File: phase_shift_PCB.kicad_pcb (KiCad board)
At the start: 2 copper layers, 9.5 x 9.5 mm, 18 parts, among them J1 132414, J2 132414, J3 Conn_01x01_Socket, J4 Conn_01x01_Socket, J5 Conn_01x01_Pin, J6 Conn_01x01_Pin, U1 OPA2134, U2 LM13700, U3 LM334M

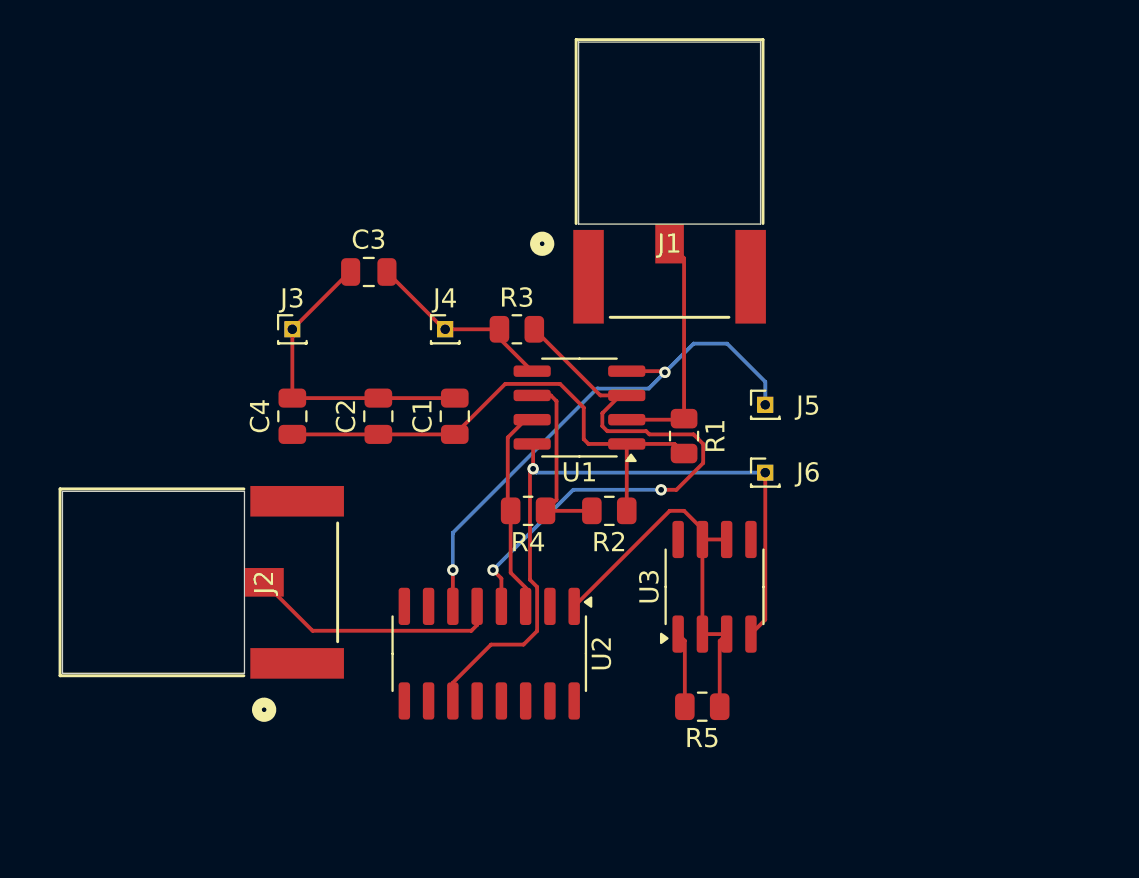
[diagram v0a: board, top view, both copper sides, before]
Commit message: Added digipots to schematic
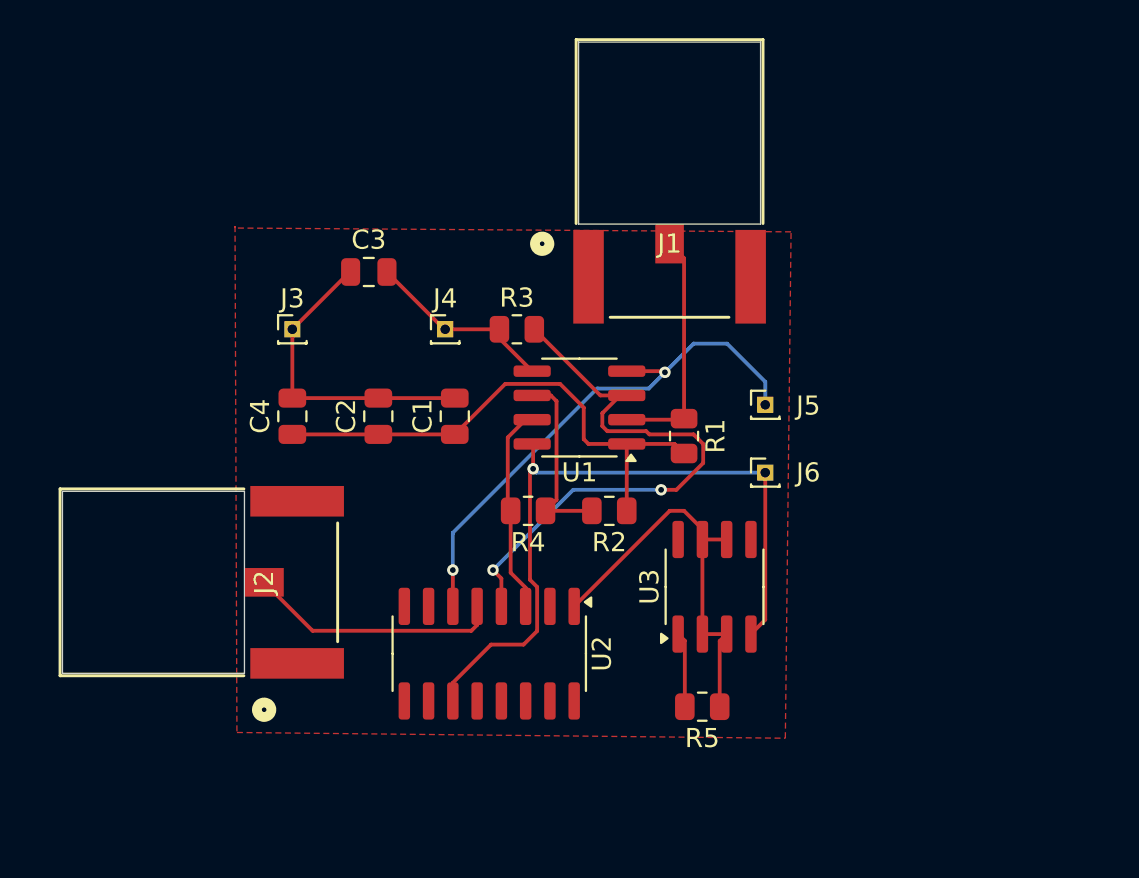
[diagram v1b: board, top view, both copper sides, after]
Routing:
- added copper zone on F.Cu, net GND
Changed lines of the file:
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@@
 		(net 22)
+	)
+	(zone
+		(net 3)
+		(net_name "GND")
+		(layer "F.Cu")
+		(hatch edge 0.5)
+		(connect_pads
+			(clearance 0.5)
+		)
+		(min_thickness 0.25)
+		(filled_areas_thickness no)
+		(fill yes
+			(thermal_gap 0.5)
+			(thermal_bridge_width 0.5)
+		)
+		(polygon
+			(pts
+				(xy 30.5 59.6) (xy 30.6 86.1) (xy 59.3 86.4) (xy 59.6 59.9) (xy 30.5 59.7)
+			)
+		)
 	)
 	(embedded_fonts no)

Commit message: PCB pretty much finished
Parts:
- removed R3: 1000, Resistor_SMD:R_0805_2012Metric
- added C5: 100n, Capacitor_SMD:C_0805_2012Metric, F.Cu at (44.4, 73.5)
- added C6: 100n, Capacitor_SMD:C_0805_2012Metric, F.Cu at (54.2, 68.3)
- added C7: 100n, Capacitor_SMD:C_0805_2012Metric, F.Cu at (41.0, 77.0)
- added C8: 100n, Capacitor_SMD:C_0805_2012Metric, F.Cu at (42.9, 87.0)
- added J10: Conn_01x01_Socket, Connector_PinHeader_1.00mm:PinHeader_1x01_P1.00mm_Vertical, F.Cu at (46.4, 57.4)
- added J11: Conn_01x01_Socket, Connector_PinHeader_1.00mm:PinHeader_1x01_P1.00mm_Vertical, F.Cu at (49.4, 57.4)
- added J12: Conn_01x01_Socket, Connector_PinHeader_1.00mm:PinHeader_1x01_P1.00mm_Vertical, F.Cu at (52.3, 57.4)
- added J13: Conn_01x01_Socket, Connector_PinHeader_1.00mm:PinHeader_1x01_P1.00mm_Vertical, F.Cu at (55.2, 57.4)
- added J5: Conn_01x01_Pin, Connector_PinHeader_1.00mm:PinHeader_1x01_P1.00mm_Vertical, F.Cu at (62.1, 73.1)
- added J8: Conn_01x01_Socket, Connector_PinHeader_1.00mm:PinHeader_1x01_P1.00mm_Vertical, F.Cu at (40.6, 57.4)
- added J9: Conn_01x01_Socket, Connector_PinHeader_1.00mm:PinHeader_1x01_P1.00mm_Vertical, F.Cu at (43.5, 57.4)
- added U4: AD8400ARZ10-REEL, Library:SOIC127P600X175-8N, F.Cu at (52.8, 62.5)
- added U5: AD8400ARZ1-REEL, Library:SOIC127P600X175-8N, F.Cu at (43.7, 62.5)
- moved J1 16.0 mm to (66.6, 65.8), turned to -90 degrees
- moved J6 7.90 mm to (62.1, 75.8)
- moved J7 7.21 mm to (62.1, 78.6)
- moved R5 5.47 mm to (58.7, 80.8), turned to -90 degrees
- moved R4 5.02 mm to (43.6, 70.0), turned to -90 degrees
- moved J4 3.54 mm to (38.1, 66.0)
- moved U3 2.50 mm to (53.7, 80.1), turned to 180 degrees
- moved C1 2.42 mm to (39.8, 70.6)
- moved C2 2.42 mm to (35.8, 70.5)
- moved C3 2.42 mm to (35.3, 63.0)
- moved C4 2.42 mm to (31.3, 70.5)
- moved J3 2.42 mm to (31.3, 66.0)
- moved R2 0.89 mm to (50.0, 73.6)
- moved U1 0.71 mm to (48.5, 69.8)
- moved R1 0.71 mm to (54.0, 71.3)
- renumbered J5 to J6, J6 to J7
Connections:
- net Net-(J4-Pin_1) renamed /W1
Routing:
- net +15V: track 37.6 -> 4.66 mm, vias 1 -> 0
- net GND: track 30.7 -> 0.00 mm, vias 2 -> 0
- net -15V: track 28.4 -> 6.82 mm, vias 2 -> 1
- net +5V: track 0.00 -> 16.3 mm, vias 0 -> 2
- net Net-(R5-Pad1): track 21.2 -> 5.71 mm
- net CLK: track 0.00 -> 14.3 mm
- net Net-(C1-Pad1): track 27.6 -> 13.6 mm
- net Net-(J2-Pad1): track 13.3 -> 0.00 mm
- net SDI: track 0.00 -> 12.8 mm, vias 0 -> 2
- net /W2: track 0.00 -> 11.1 mm
- net Net-(U1A--): track 12.5 -> 3.02 mm
- net Net-(J9-Pin_1): track 0.00 -> 9.21 mm
- net Net-(U2C-+): track 10.9 -> 2.65 mm
- net /W1: track 10.0 -> 17.3 mm
- net Net-(J11-Pin_1): track 0.00 -> 6.45 mm
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- removed copper zone on F.Cu, net GND

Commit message: .
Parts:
- J1, J2: value 132414 -> SMA-J-P-H-ST-EM1
- moved R1 0.50 mm to (53.5, 71.3)
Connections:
- J1 pad 2: (no net) -> GND
- J1 pad 3: (no net) -> GND
- J2 pad 2: (no net) -> GND
- J2 pad 3: (no net) -> GND
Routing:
- net +15V: track 4.66 -> 38.1 mm, vias 0 -> 2
- net -15V: track 6.82 -> 36.1 mm, vias 1 -> 2
- net Net-(C1-Pad1): track 13.6 -> 30.3 mm
- net Net-(J2-Pad1): track 0.00 -> 13.4 mm
- net Net-(U1A--): track 3.02 -> 14.1 mm
- net Net-(U2C-+): track 2.65 -> 13.3 mm
- net Net-(R5-Pad1): track 5.71 -> 13.2 mm
- net /W1: vias 0 -> 2
- net GND: vias 0 -> 105
- added copper zone on B.Cu, net GND
- added copper zone on F.Cu, net GND
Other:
- board size 9.5 x 9.5 mm -> 40 x 38.5 mm
- board text added: "+15V"
- board text added: "-15V"
- board text added: "5V"
- board text added: "CLK"
- board text added: "CS1"
- board text added: "CS2"
- board text added: "Dihan Wu & Hiro Shiraishi"
- board text added: "GND"
- board text added: "OPT"
- board text added: "Phase Shift PCB V1.0"
- board text added: "SDI"

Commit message: .
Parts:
- removed J10, J11, J12, J13, J9: Conn_01x01_Socket, Connector_PinHeader_1.00mm:PinHeader_1x01_P1.00mm_Vertical
- J3, J4: value Conn_01x01_Socket -> Conn_01x01_Pin; footprint Connector_PinHeader_1.00mm:PinHeader_1x01_P1.00mm_Vertical -> Connector_PinHeader_2.54mm:PinHeader_1x01_P2.54mm_Vertical
- J5, J6, J7: footprint Connector_PinHeader_1.00mm:PinHeader_1x01_P1.00mm_Vertical -> Connector_PinHeader_2.54mm:PinHeader_1x01_P2.54mm_Vertical
- J8: value Conn_01x01_Socket -> Conn_01x06_Pin; footprint Connector_PinHeader_1.00mm:PinHeader_1x01_P1.00mm_Vertical -> Connector_PinSocket_2.54mm:PinSocket_1x06_P2.54mm_Vertical
- moved J7 6.21 mm to (65.5, 83.8)
- moved J6 4.63 mm to (65.5, 79.0)
- moved J5 3.57 mm to (65.5, 74.2)
- moved J8 3.01 mm to (41.7, 54.6), turned to 90 degrees
- moved C3 1.80 mm to (34.3, 61.5)
- moved J3 1.28 mm to (30.5, 65.0)
- moved J4 1.00 mm to (38.0, 65.0)
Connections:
- U4 pad 3: Net-(J12-Pin_1) -> CS2
- U5 pad 3: Net-(J10-Pin_1) -> CS1
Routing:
- net CS2: track 0.00 -> 9.97 mm
- net Net-(J12-Pin_1): track 9.21 -> 0.00 mm
- net CS1: track 0.00 -> 8.80 mm
- net Net-(J10-Pin_1): track 6.45 -> 0.00 mm
- net +15V: track 38.1 -> 43.8 mm
- net -15V: track 36.1 -> 40.8 mm
- net +5V: track 16.3 -> 18.8 mm
- net SDI: track 12.8 -> 15.3 mm
- net Net-(J3-Pin_1): track 16.4 -> 18.1 mm
- net /W1: track 17.3 -> 17.9 mm
- net CLK: track 14.3 -> 14.5 mm, vias 0 -> 2
- net GND: vias 105 -> 81
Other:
- board size 40 x 38.5 mm -> 40 x 39 mm

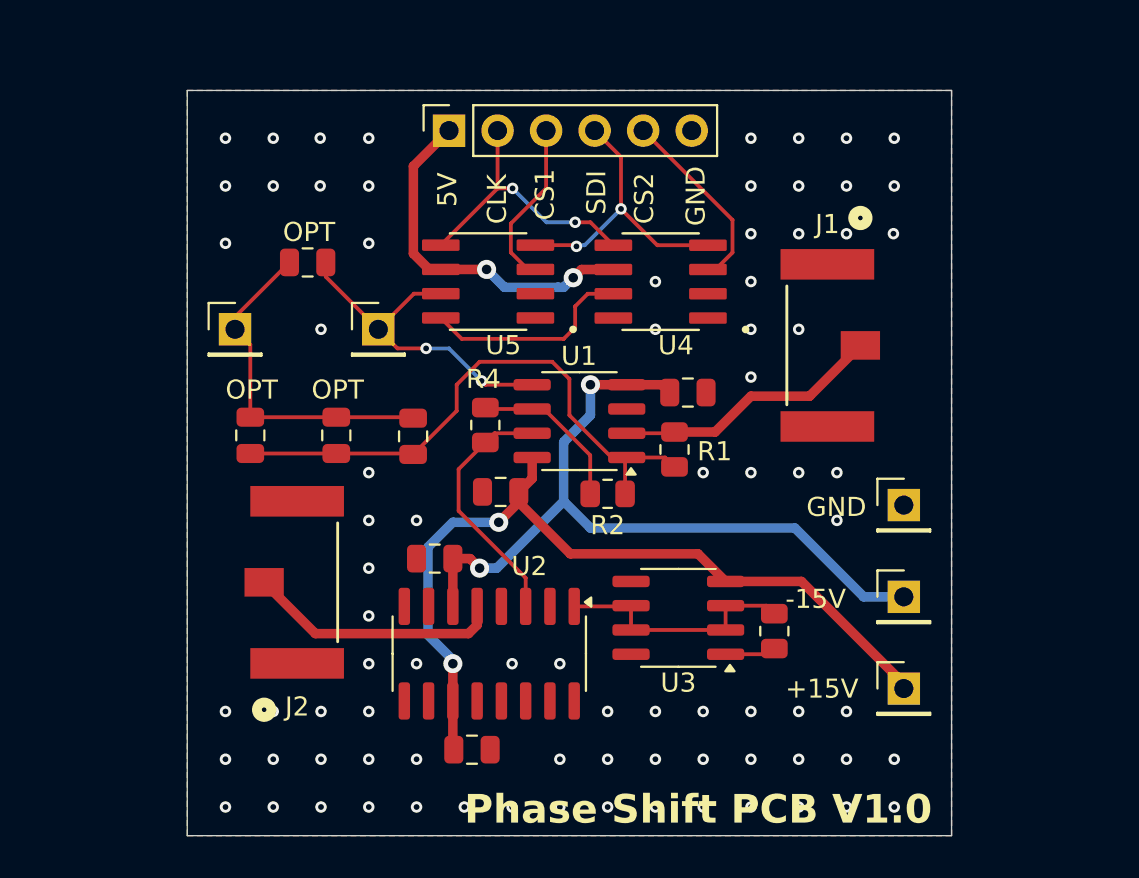
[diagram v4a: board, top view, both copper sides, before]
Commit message: Changed to use mouser SMA connectors
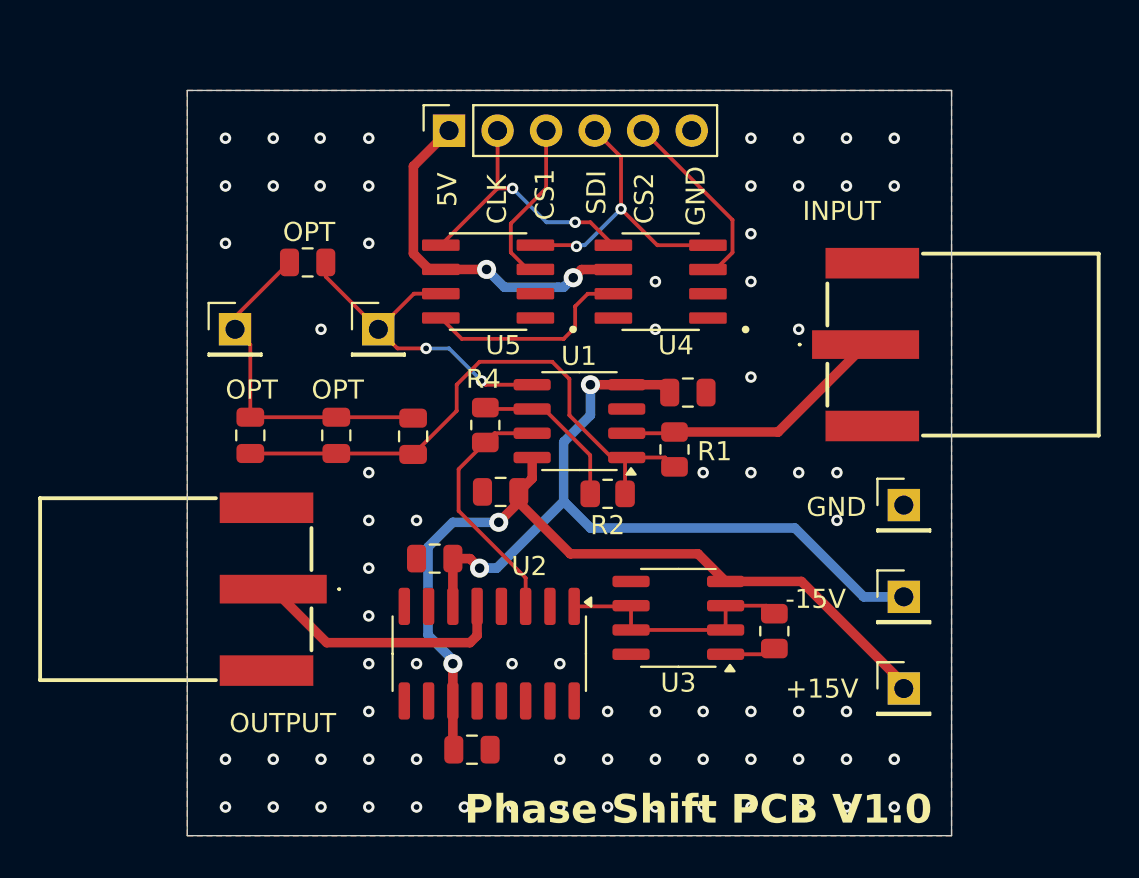
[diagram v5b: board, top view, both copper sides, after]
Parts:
- J1, J2: value SMA-J-P-H-ST-EM1 -> CONSMA020.062-G; footprint Library:CONN_132414_AMP -> Library:CONSMA020062G
- moved J1 1.96 mm to (68.6, 65.8), turned to 90 degrees
- moved J2 1.26 mm to (27.4, 78.6), turned to -90 degrees
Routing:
- net GND: vias 81 -> 74
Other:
- board text added: "INPUT"
- board text added: "OUTPUT"
